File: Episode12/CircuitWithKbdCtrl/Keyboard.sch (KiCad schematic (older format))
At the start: 11 parts, among them J501 Conn_01x20, U501 P80C32SBPN, U502 IDT7201, U503 74LS138, U504 74HCT541

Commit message: more work on keyboard controller
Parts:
- added C506: 22pF, symbol device:C
- added Y501: 11.0592 MHz, symbol device:Crystal
- C505: value 100nF -> 22pF
- U501: value P80C32SBPN -> 87C51/89C51
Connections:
- net labels added: RST
- wire segments 161 -> 173
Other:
- note added: "Buffer to allow EF (empty flag)\nand FF (full flag) bits of FIFO\nto be read by the CPU."
- note added: "Port 0 reads the columns\n(with pull down resistors\nkeeping the column inputs\nat ground unless a keyswitch\nhas made a connection to a\nrow when the row scan is in\nprogress)"
- note added: "Port 1 actively\ndrives the rows\nof the keyboard\nmatrix"
- note added: "Port 2 is used for\nsending scan code\ndata to the FIFO\nchip."
- note removed: "Port 0 reads the\nrows (with pull down\nresistors keeping\nthe row inputs at\nground unless a\nkeyswitch has made\na connection to\na column when the\ncolumn scan is in\nprogress)"
- note removed: "Port 1 actively\ndrives the columns\nof the keyboard\nmatrix"
- note removed: "Port 3 is used for\nsending scan code\ndata to the FIFO\nchip."
- moved on the sheet: C501, C502, C503, C504, J501, RN501, U501, U503

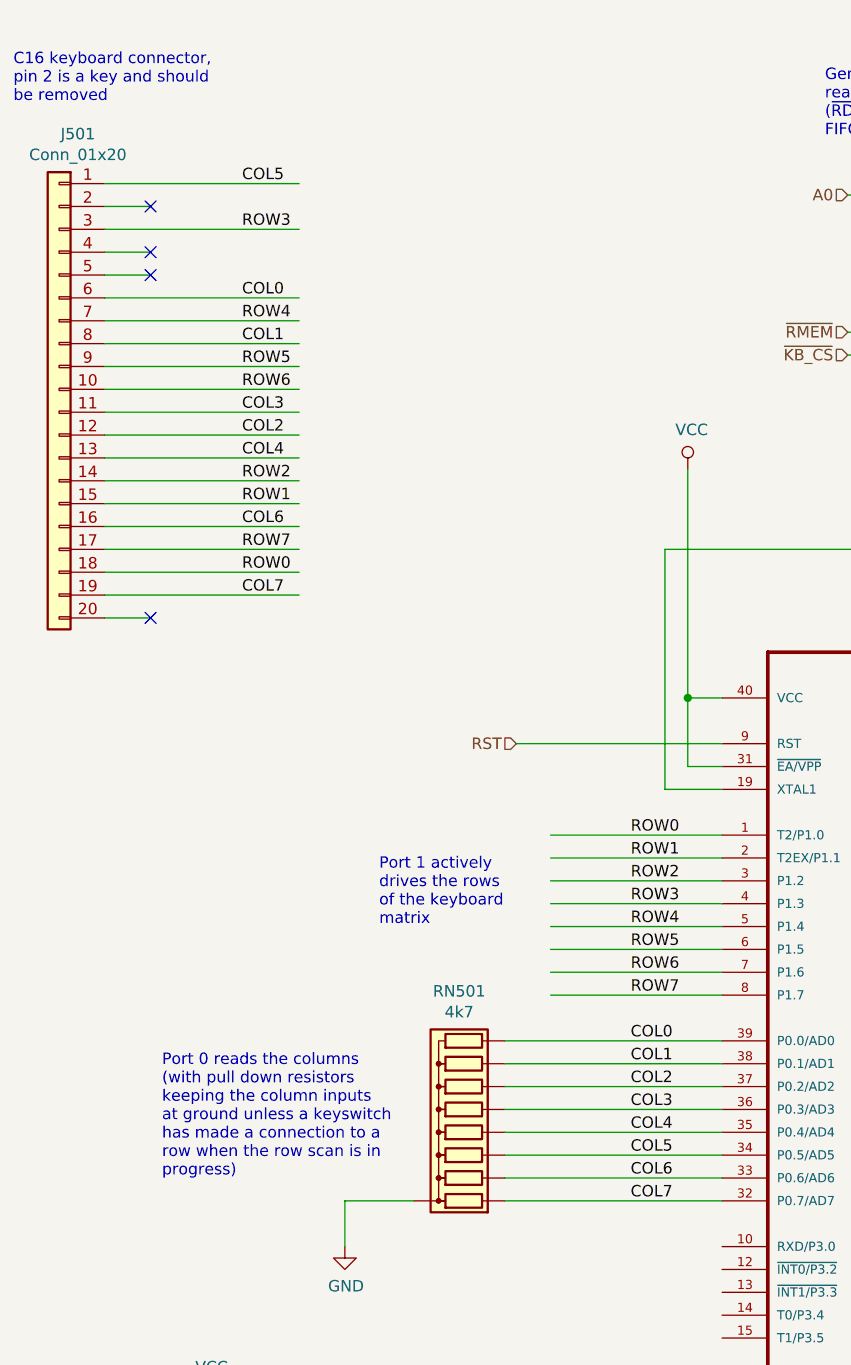
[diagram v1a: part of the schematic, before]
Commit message: fixed keyboard rows and columns being reversed
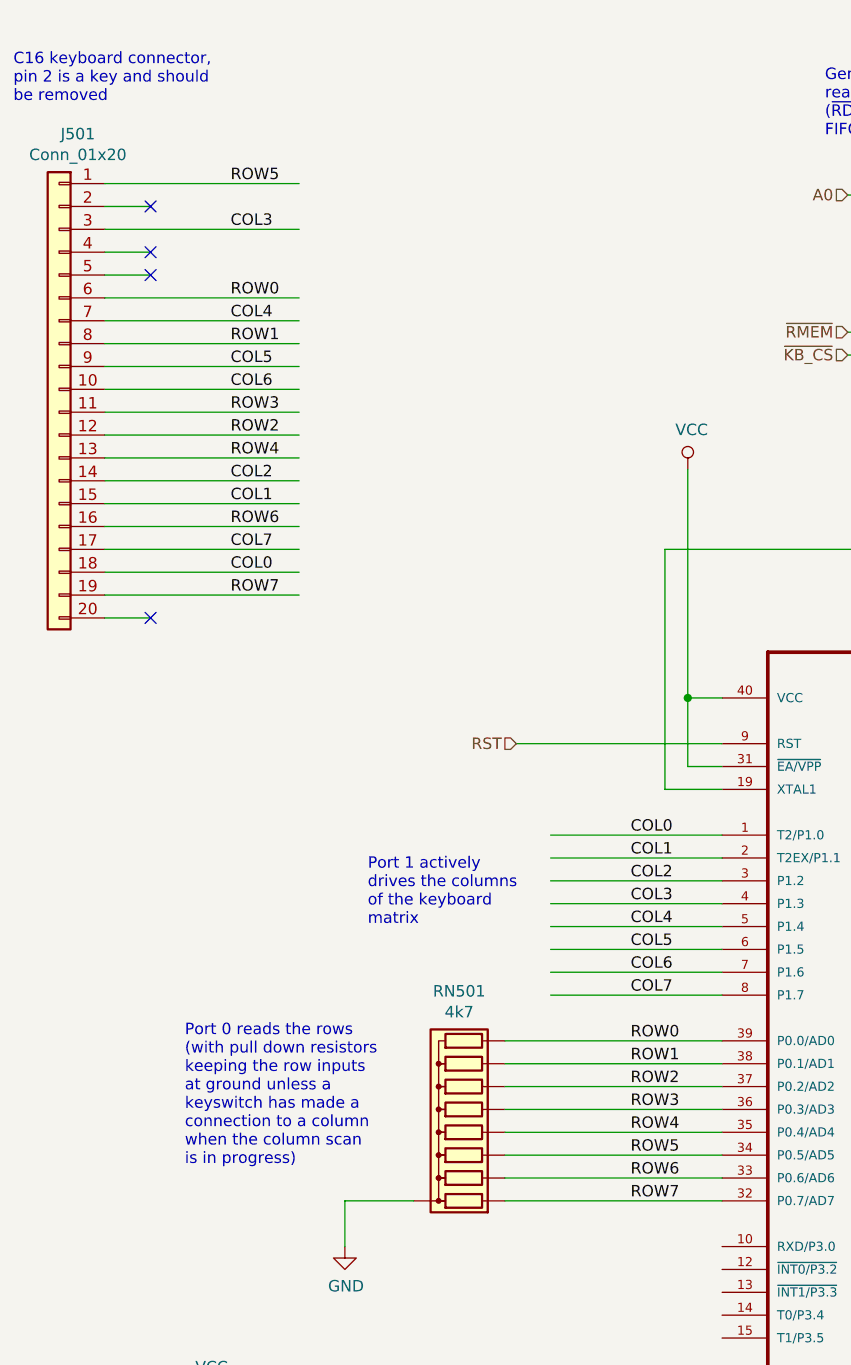
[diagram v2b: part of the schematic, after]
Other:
- note added: "Port 0 reads the rows\n(with pull down resistors\nkeeping the row inputs\nat ground unless a\nkeyswitch has made a\nconnection to a column\nwhen the column scan\nis in progress)"
- note added: "Port 1 actively\ndrives the columns\nof the keyboard\nmatrix"
- note removed: "Port 0 reads the columns\n(with pull down resistors\nkeeping the column inputs\nat ground unless a keyswitch\nhas made a connection to a\nrow when the row scan is in\nprogress)"
- note removed: "Port 1 actively\ndrives the rows\nof the keyboard\nmatrix"
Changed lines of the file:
@@
 	1100 1650 1300 1650
 NoConn ~ 1300 1650
-Text Label 1700 1750 0    50   ~ 0
-COL0
-Text Label 1700 1950 0    50   ~ 0
-COL1
-Text Label 1700 2350 0    50   ~ 0
-COL2
-Text Label 1700 2250 0    50   ~ 0
-COL3
-Text Label 1700 2450 0    50   ~ 0
-COL4
-Text Label 1700 1250 0    50   ~ 0
-COL5
-Text Label 1700 2750 0    50   ~ 0
-COL6
-Text Label 1700 3050 0    50   ~ 0
-COL7
 Wire Wire Line
 	1100 3150 1300 3150
 NoConn ~ 1300 3150
+Text Label 3400 4100 0    50   ~ 0
+COL0
+Text Label 3400 4200 0    50   ~ 0
+COL1
+Text Label 3400 4300 0    50   ~ 0
+COL2
+Text Label 3400 4400 0    50   ~ 0
+COL3
+Text Label 3400 4500 0    50   ~ 0
+COL4
+Text Label 3400 4600 0    50   ~ 0
+COL5
+Text Label 3400 4700 0    50   ~ 0
+COL6
+Text Label 3400 4800 0    50   ~ 0
+COL7
 Text Label 3400 5000 0    50   ~ 0
-COL0
+ROW0
 Text Label 3400 5100 0    50   ~ 0
-COL1
+ROW1
 Text Label 3400 5200 0    50   ~ 0
-COL2
+ROW2
 Text Label 3400 5300 0    50   ~ 0
-COL3
+ROW3
 Text Label 3400 5400 0    50   ~ 0
-COL4
+ROW4
 Text Label 3400 5500 0    50   ~ 0
-COL5
+ROW5
 Text Label 3400 5600 0    50   ~ 0
-COL6
+ROW6
 Text Label 3400 5700 0    50   ~ 0
-COL7
-Text Label 1700 2950 0    50   ~ 0
-ROW0
-Text Label 1700 2650 0    50   ~ 0
-ROW1
-Text Label 1700 2550 0    50   ~ 0
-ROW2
-Text Label 1700 1450 0    50   ~ 0
-ROW3
-Text Label 1700 1850 0    50   ~ 0
-ROW4
-Text Label 1700 2050 0    50   ~ 0
-ROW5
-Text Label 1700 2150 0    50   ~ 0
-ROW6
-Text Label 1700 2850 0    50   ~ 0
-ROW7
-Text Label 3400 4100 0    50   ~ 0
-ROW0
-Text Label 3400 4200 0    50   ~ 0
-ROW1
-Text Label 3400 4300 0    50   ~ 0
-ROW2
-Text Label 3400 4400 0    50   ~ 0
-ROW3
-Text Label 3400 4500 0    50   ~ 0
-ROW4
-Text Label 3400 4600 0    50   ~ 0
-ROW5
-Text Label 3400 4700 0    50   ~ 0
-ROW6
-Text Label 3400 4800 0    50   ~ 0
 ROW7
 $Comp
@@
 $EndComp
 Wire Wire Line
-	1100 2950 1950 2950
-Wire Wire Line
-	1100 1450 1950 1450
-Wire Wire Line
-	1100 1850 1950 1850
-Wire Wire Line
-	1100 2050 1950 2050
-Wire Wire Line
-	1100 2150 1950 2150
-Wire Wire Line
-	1100 2550 1950 2550
-Wire Wire Line
-	1100 2650 1950 2650
-Wire Wire Line
-	1100 2850 1950 2850
-Wire Wire Line
 	2450 5700 2150 5700
 Wire Wire Line
@@
 $EndComp
 Wire Wire Line
-	2850 5000 3800 5000
-Wire Wire Line
-	1100 1750 1950 1750
-Wire Wire Line
-	2850 5100 3800 5100
-Wire Wire Line
-	1100 1950 1950 1950
-Wire Wire Line
-	2850 5200 3800 5200
-Wire Wire Line
-	2850 5300 3800 5300
-Wire Wire Line
-	1100 2450 1950 2450
-Wire Wire Line
-	2850 5400 3800 5400
-Wire Wire Line
-	1100 1250 1950 1250
-Wire Wire Line
-	2850 5500 3800 5500
-Wire Wire Line
-	1100 2750 1950 2750
-Wire Wire Line
-	2850 5600 3800 5600
-Wire Wire Line
-	2850 5700 3800 5700
-Wire Wire Line
-	1100 3050 1950 3050
+	3050 4100 3800 4100
+Wire Wire Line
+	3050 4200 3800 4200
+Wire Wire Line
+	3050 4300 3800 4300
+Wire Wire Line
+	3050 4400 3800 4400
+Wire Wire Line
+	3050 4500 3800 4500
+Wire Wire Line
+	3050 4600 3800 4600
+Wire Wire Line
+	3050 4700 3800 4700
+Wire Wire Line
+	3050 4800 3800 4800
 Text Notes 700  900  0    50   ~ 0
 C16 keyboard connector,\npin 2 is a key and should\nbe removed
@@
 $EndComp
 Wire Wire Line
-	1100 2250 1950 2250
-Wire Wire Line
-	1100 2350 1950 2350
-Wire Wire Line
 	2150 5700 2150 5900
 $Comp
@@
 $EndComp
 Wire Wire Line
-	3050 4200 3800 4200
-Wire Wire Line
-	3050 4300 3800 4300
-Wire Wire Line
-	3050 4400 3800 4400
-Wire Wire Line
-	3050 4500 3800 4500
-Wire Wire Line
-	3050 4700 3800 4700
-Wire Wire Line
-	3050 4800 3800 4800
-Wire Wire Line
-	3050 4100 3800 4100
-Wire Wire Line
-	3050 4600 3800 4600
-Text Notes 2300 4500 0    50   ~ 0
-Port 1 actively\ndrives the rows\nof the keyboard\nmatrix
-Text Notes 1350 5600 0    50   ~ 0
-Port 0 reads the columns\n(with pull down resistors\nkeeping the column inputs\nat ground unless a keyswitch\nhas made a connection to a\nrow when the row scan is in\nprogress)
+	2850 5100 3800 5100
+Wire Wire Line
+	2850 5200 3800 5200
+Wire Wire Line
+	2850 5300 3800 5300
+Wire Wire Line
+	2850 5400 3800 5400
+Wire Wire Line
+	2850 5600 3800 5600
+Wire Wire Line
+	2850 5700 3800 5700
+Wire Wire Line
+	2850 5000 3800 5000
+Wire Wire Line
+	2850 5500 3800 5500
+Text Notes 2250 4500 0    50   ~ 0
+Port 1 actively\ndrives the columns\nof the keyboard\nmatrix
+Text Notes 1450 5550 0    50   ~ 0
+Port 0 reads the rows\n(with pull down resistors\nkeeping the row inputs\nat ground unless a\nkeyswitch has made a\nconnection to a column\nwhen the column scan\nis in progress)
 Text Label 6600 4300 0    50   ~ 0
 SCDAT0
@@
 Wire Wire Line
 	6650 3200 6800 3200
-Wire Bus Line
-	7150 1550 7150 4900
-Wire Bus Line
-	9800 1550 9800 6550
 Connection ~ 6800 3200
 Wire Wire Line
@@
 	1    0    0    -1
 $EndComp
+Text Label 1650 2950 0    50   ~ 0
+COL0
+Text Label 1650 2650 0    50   ~ 0
+COL1
+Text Label 1650 2550 0    50   ~ 0
+COL2
+Text Label 1650 1450 0    50   ~ 0
+COL3
+Text Label 1650 1850 0    50   ~ 0
+COL4
+Text Label 1650 2150 0    50   ~ 0
+COL6
+Text Label 1650 2850 0    50   ~ 0
+COL7
+Text Label 1650 1750 0    50   ~ 0
+ROW0
+Text Label 1650 1950 0    50   ~ 0
+ROW1
+Text Label 1650 2350 0    50   ~ 0
+ROW2
+Text Label 1650 2250 0    50   ~ 0
+ROW3
+Text Label 1650 2450 0    50   ~ 0
+ROW4
+Text Label 1650 1250 0    50   ~ 0
+ROW5
+Text Label 1650 2750 0    50   ~ 0
+ROW6
+Text Label 1650 3050 0    50   ~ 0
+ROW7
+Wire Wire Line
+	1100 2950 1950 2950
+Wire Wire Line
+	1100 1450 1950 1450
+Wire Wire Line
+	1100 1850 1950 1850
+Wire Wire Line
+	1100 2050 1950 2050
+Wire Wire Line
+	1100 2150 1950 2150
+Wire Wire Line
+	1100 2550 1950 2550
+Wire Wire Line
+	1100 2650 1950 2650
+Wire Wire Line
+	1100 2850 1950 2850
+Wire Wire Line
+	1100 1750 1950 1750
+Wire Wire Line
+	1100 1950 1950 1950
+Wire Wire Line
+	1100 2450 1950 2450
+Wire Wire Line
+	1100 1250 1950 1250
+Wire Wire Line
+	1100 2750 1950 2750
+Wire Wire Line
+	1100 3050 1950 3050
+Wire Wire Line
+	1100 2250 1950 2250
+Wire Wire Line
+	1100 2350 1950 2350
+Text Label 1650 2050 0    50   ~ 0
+COL5
+Wire Bus Line
+	7150 1550 7150 4900
+Wire Bus Line
+	9800 1550 9800 6550
 $EndSCHEMATC

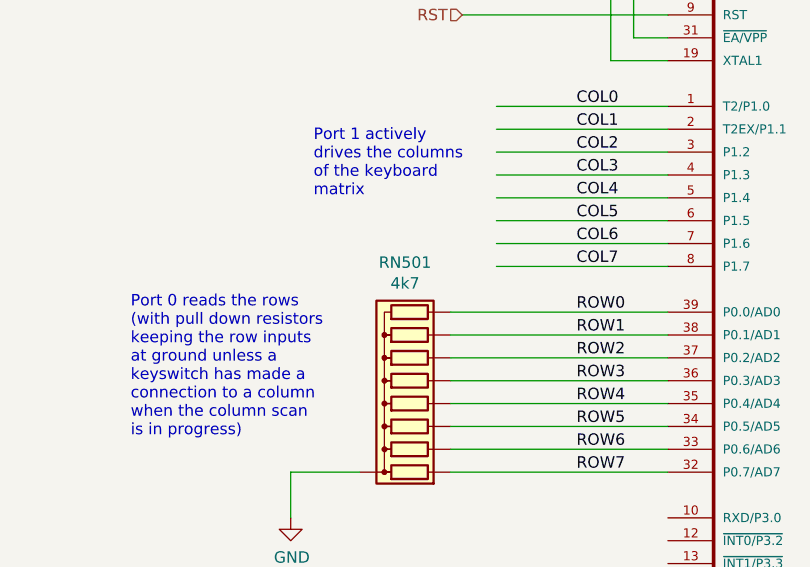
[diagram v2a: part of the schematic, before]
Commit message: pull-down resistors need to be weaker
The port 1 output pins on an 89C51 can't overcome
a 4.7k resistor tied to ground.  15k and up seem to
work.  Plan to use 22k resistors, hopefully that
will be good for an actual 87C51.  I think weak pull
downs should be fine because we don't require fast
transitions.
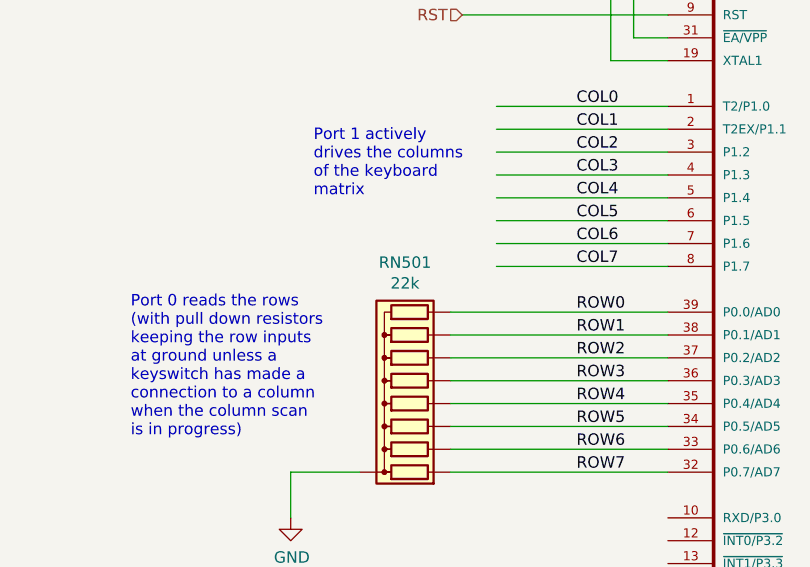
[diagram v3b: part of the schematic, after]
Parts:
- RN501: value 4k7 -> 22k
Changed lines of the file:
@@
 P 2650 5300
 F 0 "RN501" V 3167 5300 50  0000 C CNN
-F 1 "4k7" V 3076 5300 50  0000 C CNN
+F 1 "22k" V 3076 5300 50  0000 C CNN
 F 2 "Resistors_THT:R_Array_SIP9" V 3125 5300 50  0001 C CNN
 F 3 "" H 2650 5300 50  0001 C CNN
